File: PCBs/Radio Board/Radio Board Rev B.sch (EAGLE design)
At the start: 5 parts, among them T2 AD590KRZ

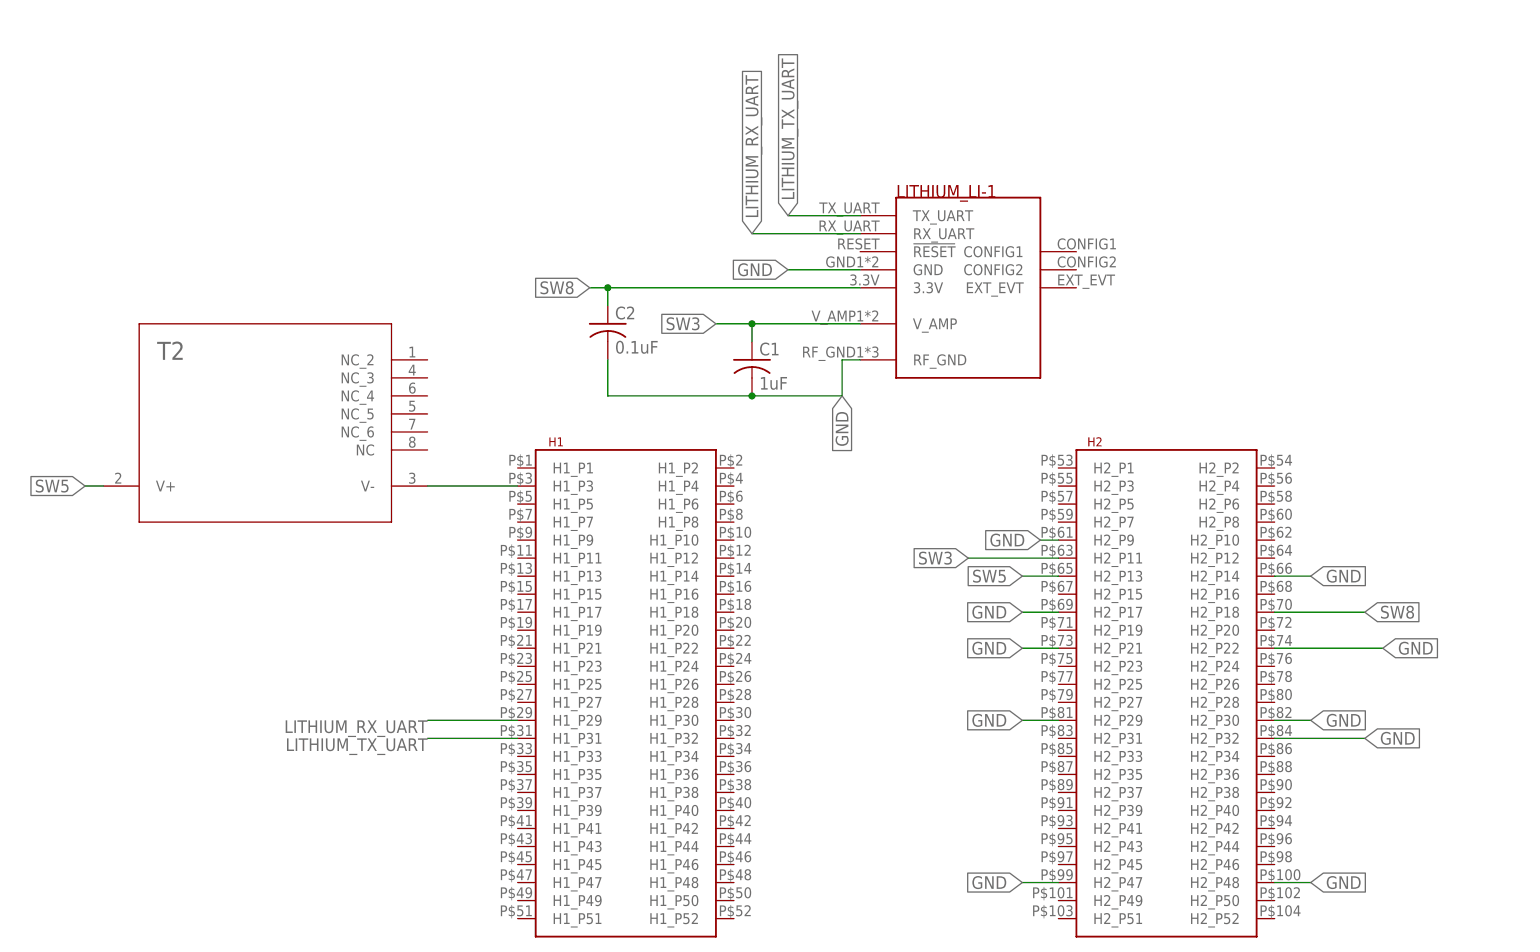
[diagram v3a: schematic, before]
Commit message: Remove temp sensor, tweak trace width
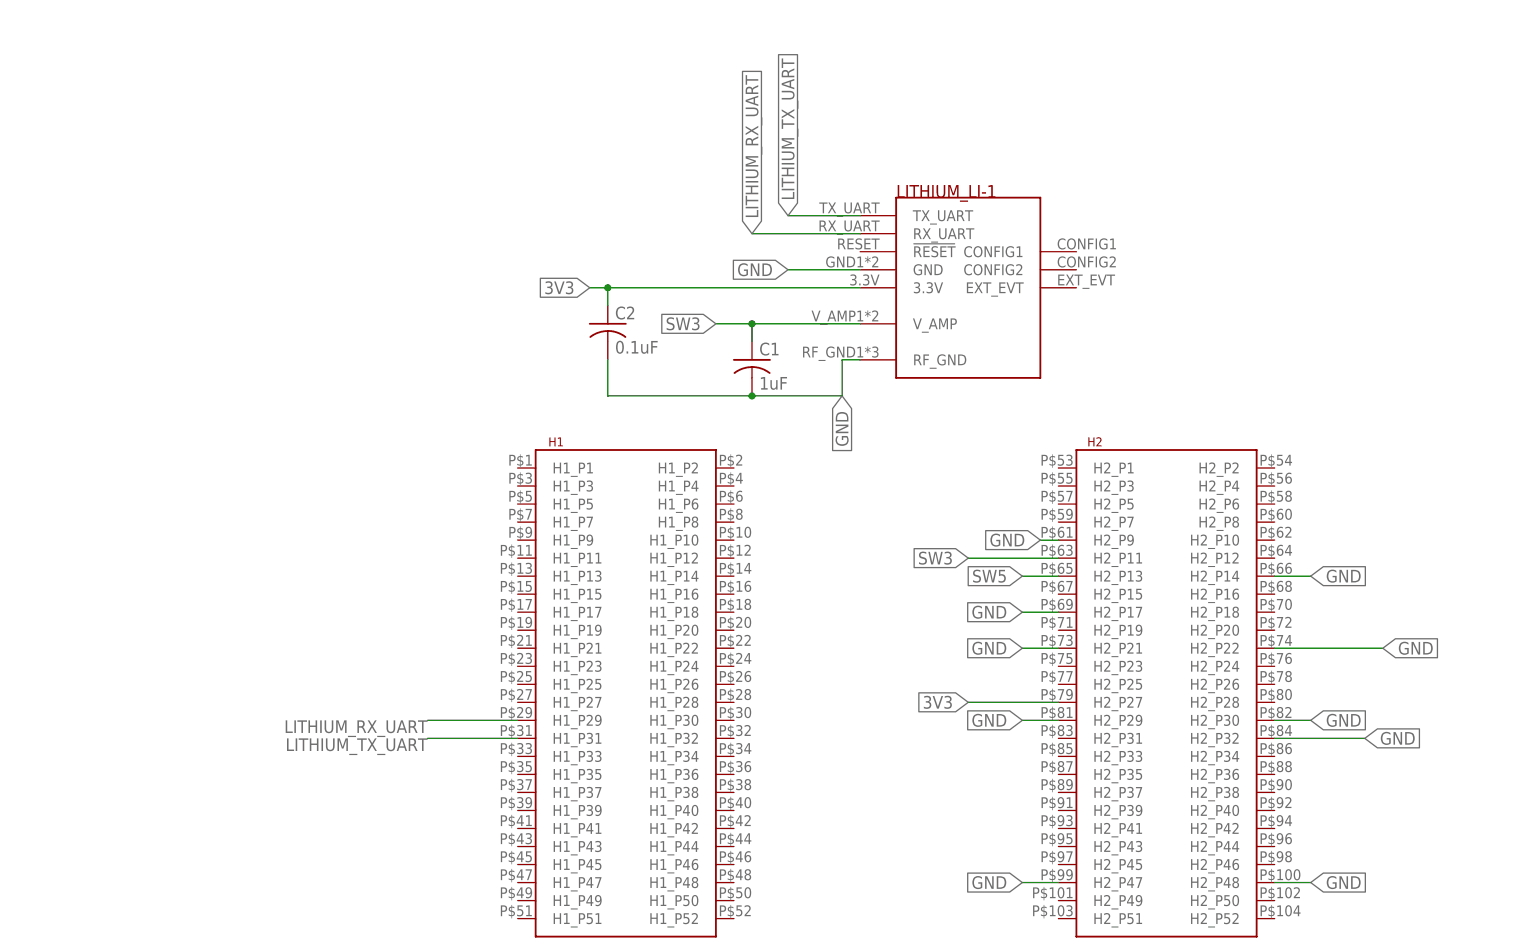
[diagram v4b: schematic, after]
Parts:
- removed T2: AD590KRZ, AD590KRZ:AD590KRZ
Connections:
- removed net N$1: T2.V-, U$2.H1_P3
- removed net SW8: C2.1, U$1.3.3V, U$2.H2_P18
- new net 3V3: C2.1, U$1.3.3V, U$2.H2_P27
- net SW5: no longer T2.V+
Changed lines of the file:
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@@
 <part name="C1" library="resistor" library_urn="urn:adsk.eagle:library:348" deviceset="C-US" device="C0805" package3d_urn="urn:adsk.eagle:package:26137/1" value="1uF"/>
 <part name="C2" library="resistor" library_urn="urn:adsk.eagle:library:348" deviceset="C-US" device="C0805" package3d_urn="urn:adsk.eagle:package:26137/1" value="0.1uF"/>
-<part name="T2" library="AD590KRZ" deviceset="AD590KRZ" device=""/>
 </parts>
 <sheets>
@@
 <instance part="C1" gate="G$1" x="55.88" y="81.28"/>
 <instance part="C2" gate="G$1" x="35.56" y="86.36"/>
-<instance part="T2" gate="A" x="-30.48" y="58.42"/>
 </instances>
 <busses>
@@
 </segment>
 </net>
-<net name="SW8" class="0">
-<segment>
-<pinref part="U$2" gate="G$1" pin="H2_P18"/>
-<wire x1="129.54" y1="45.72" x2="142.24" y2="45.72" width="0.1524" layer="91"/>
-<label x="142.24" y="45.72" size="1.778" layer="95" xref="yes"/>
-</segment>
-<segment>
-<pinref part="U$1" gate="G$1" pin="3.3V"/>
-<wire x1="71.12" y1="91.44" x2="35.56" y2="91.44" width="0.1524" layer="91"/>
-<label x="33.02" y="91.44" size="1.778" layer="95" rot="R180" xref="yes"/>
-<pinref part="C2" gate="G$1" pin="1"/>
-<wire x1="35.56" y1="91.44" x2="33.02" y2="91.44" width="0.1524" layer="91"/>
-<wire x1="35.56" y1="91.44" x2="35.56" y2="88.9" width="0.1524" layer="91"/>
-<junction x="35.56" y="91.44"/>
-</segment>
-</net>
 <net name="LITHIUM_TX_UART" class="0">
 <segment>
@@
 <label x="93.98" y="50.8" size="1.778" layer="95" rot="R180" xref="yes"/>
 </segment>
+</net>
+<net name="3V3" class="0">
 <segment>
-<pinref part="T2" gate="A" pin="V+"/>
-<wire x1="-35.56" y1="63.5" x2="-38.1" y2="63.5" width="0.1524" layer="91"/>
-<label x="-38.1" y="63.5" size="1.778" layer="95" rot="R180" xref="yes"/>
+<pinref part="U$2" gate="G$1" pin="H2_P27"/>
+<wire x1="99.06" y1="33.02" x2="86.36" y2="33.02" width="0.1524" layer="91"/>
+<label x="86.36" y="33.02" size="1.778" layer="95" rot="R180" xref="yes"/>
+</segment>
+<segment>
+<pinref part="U$1" gate="G$1" pin="3.3V"/>
+<wire x1="71.12" y1="91.44" x2="35.56" y2="91.44" width="0.1524" layer="91"/>
+<pinref part="C2" gate="G$1" pin="1"/>
+<wire x1="35.56" y1="91.44" x2="35.56" y2="88.9" width="0.1524" layer="91"/>
+<wire x1="35.56" y1="91.44" x2="33.02" y2="91.44" width="0.1524" layer="91"/>
+<junction x="35.56" y="91.44"/>
+<label x="33.02" y="91.44" size="1.778" layer="95" rot="R180" xref="yes"/>
 </segment>
 </net>
-<net name="N$1" class="0">
-<segment>
-<pinref part="T2" gate="A" pin="V-"/>
-<pinref part="U$2" gate="G$1" pin="H1_P3"/>
-<wire x1="10.16" y1="63.5" x2="22.86" y2="63.5" width="0.1524" layer="91"/>
-</segment>
-</net>

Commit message: Added Lithium OA system reset
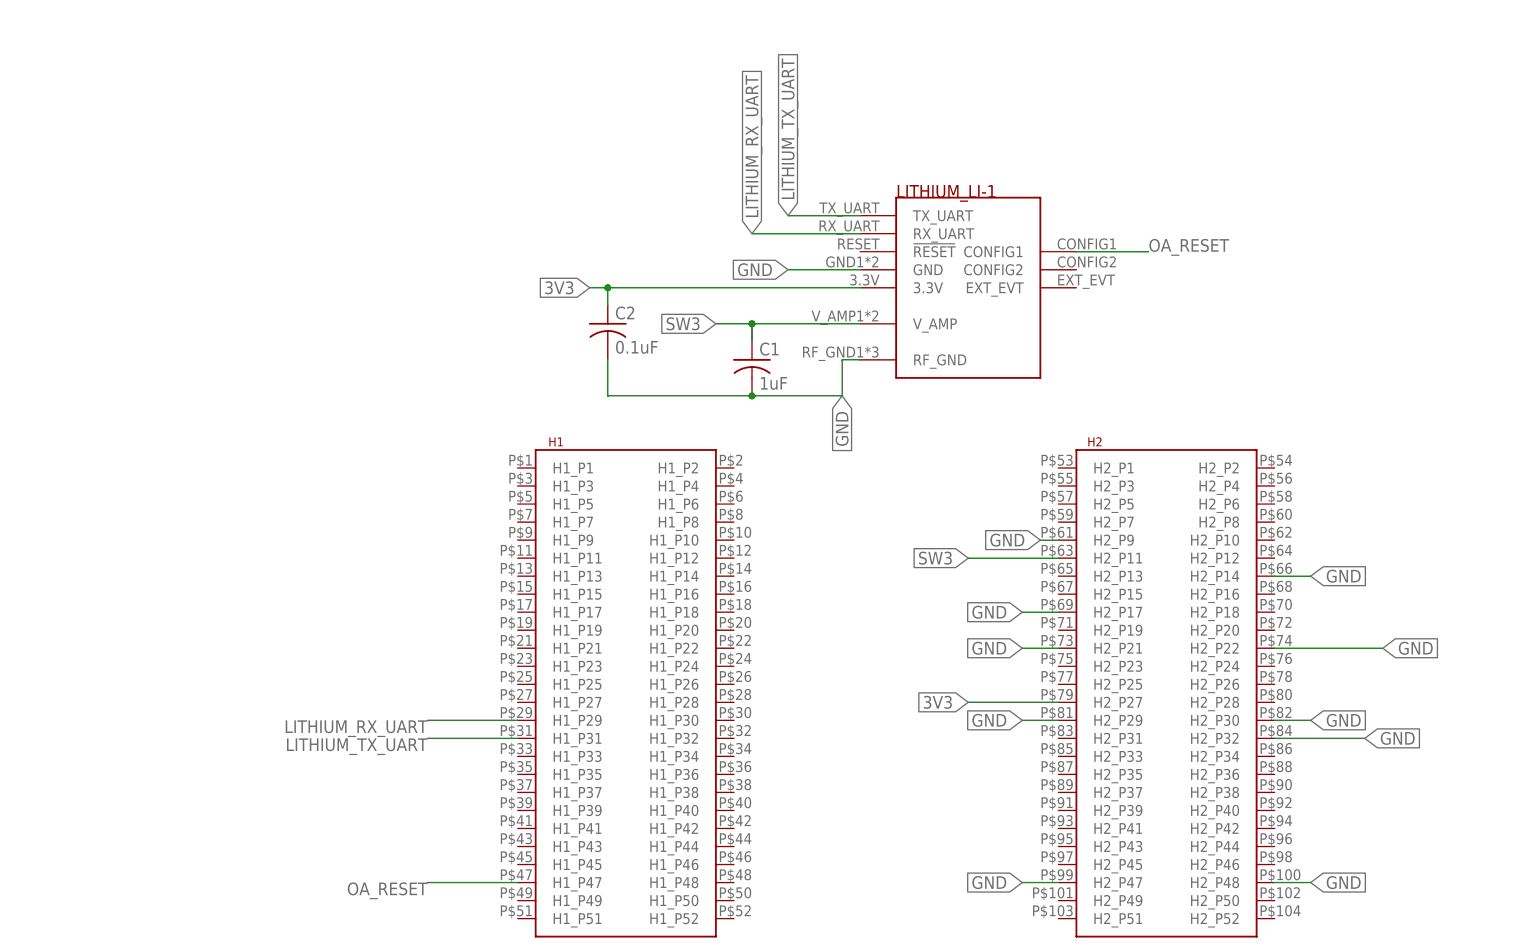
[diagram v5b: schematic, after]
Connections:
- removed net SW5: U$2.H2_P13
- new net OA_RESET: U$1.CONFIG1, U$2.H1_P47
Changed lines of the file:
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@@
-</segment>
-</net>
-<net name="SW5" class="0">
-<segment>
-<pinref part="U$2" gate="G$1" pin="H2_P13"/>
-<wire x1="99.06" y1="50.8" x2="93.98" y2="50.8" width="0.1524" layer="91"/>
-<label x="93.98" y="50.8" size="1.778" layer="95" rot="R180" xref="yes"/>
 </segment>
 </net>
@@
 </segment>
 </net>
+<net name="OA_RESET" class="0">
+<segment>
+<pinref part="U$1" gate="G$1" pin="CONFIG1"/>
+<wire x1="101.6" y1="96.52" x2="111.76" y2="96.52" width="0.1524" layer="91"/>
+<label x="111.76" y="96.52" size="1.778" layer="95"/>
+</segment>
+<segment>
+<pinref part="U$2" gate="G$1" pin="H1_P47"/>
+<wire x1="22.86" y1="7.62" x2="10.16" y2="7.62" width="0.1524" layer="91"/>
+<label x="10.16" y="7.62" size="1.778" layer="95" rot="R180"/>
+</segment>
+</net>
